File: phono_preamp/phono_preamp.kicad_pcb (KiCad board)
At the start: 2 copper layers, 30 parts, among them U1 NE5532, U2 NE5532

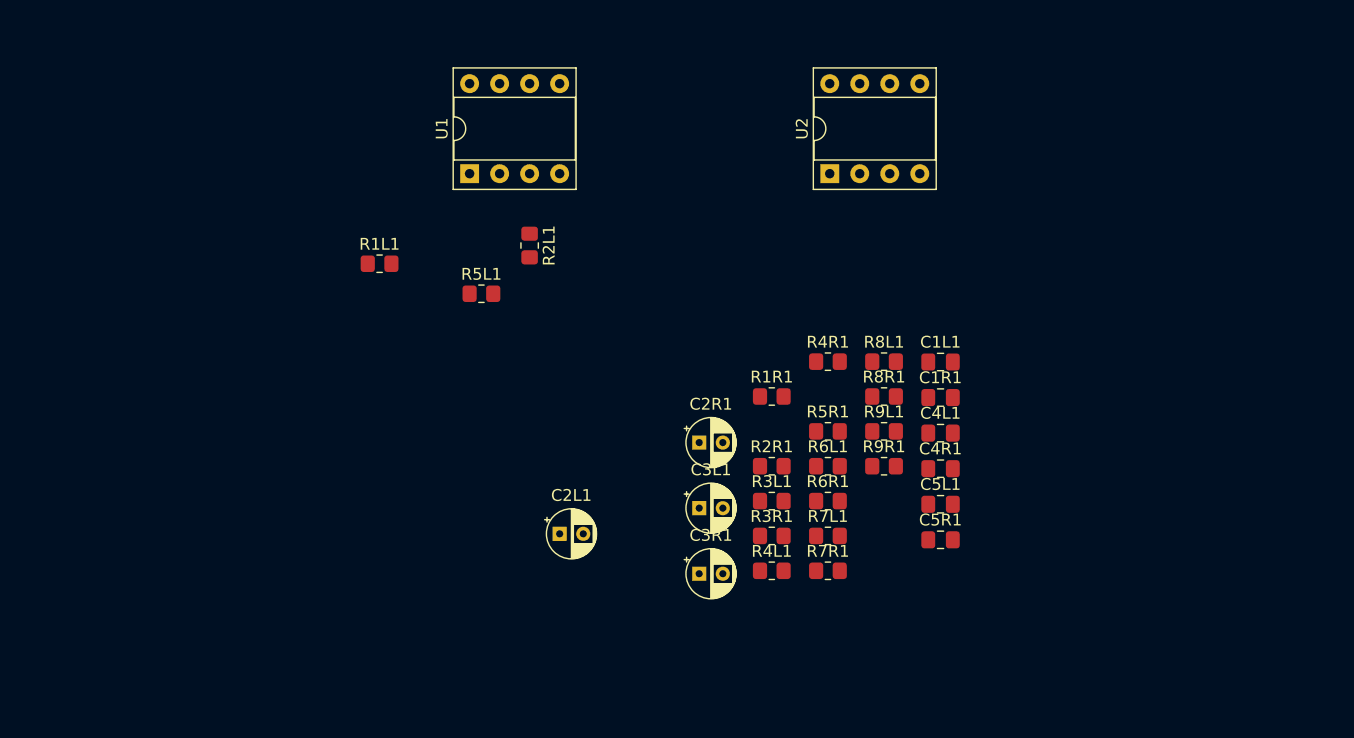
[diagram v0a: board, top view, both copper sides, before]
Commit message: testing some routing options
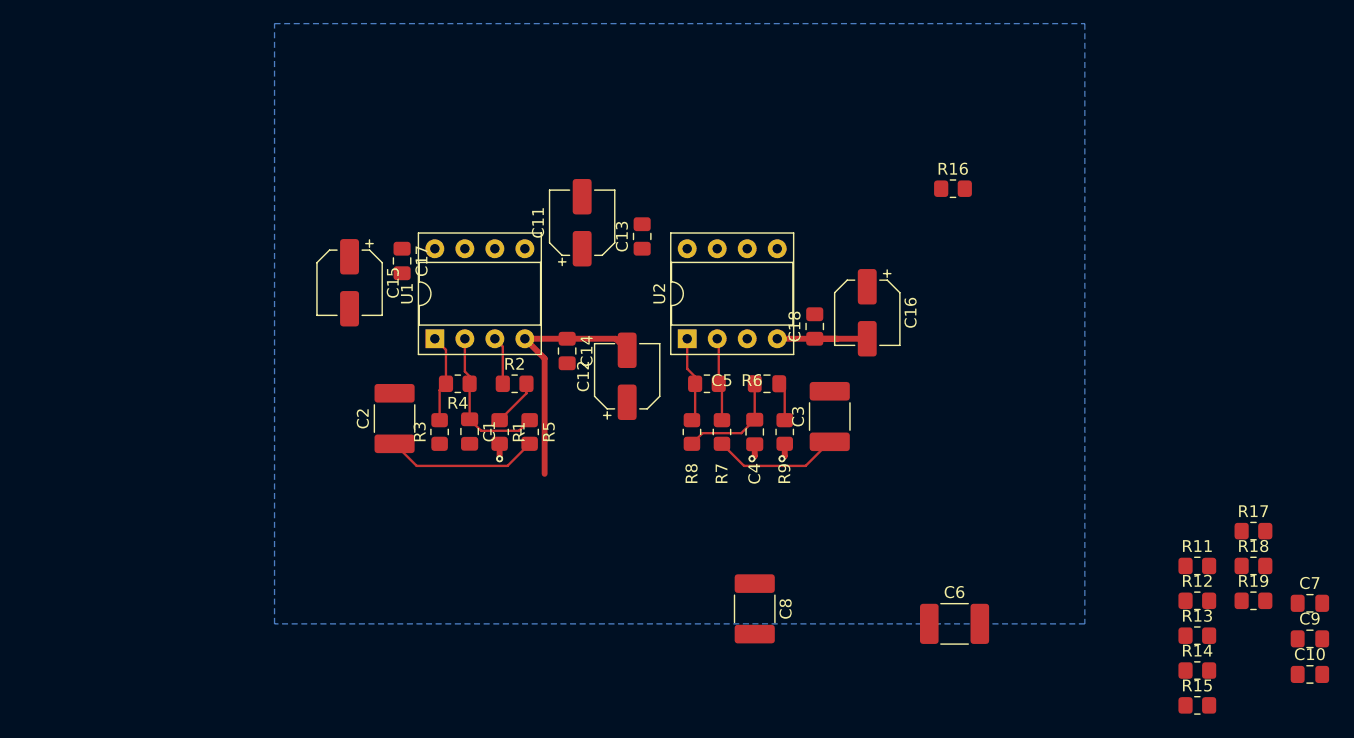
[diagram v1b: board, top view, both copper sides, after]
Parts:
- removed C1L1, C1R1: 22n, Capacitor_SMD:C_0805_2012Metric_Pad1.18x1.45mm_HandSolder
- removed C2L1, C2R1, C3L1, C3R1: 22u, Capacitor_THT:CP_Radial_D4.0mm_P2.00mm
- removed C4L1, C4R1: 100n, Capacitor_SMD:C_0805_2012Metric_Pad1.18x1.45mm_HandSolder
- removed C5L1, C5R1: 1u, Capacitor_SMD:C_0805_2012Metric_Pad1.18x1.45mm_HandSolder
- removed R1L1, R1R1: 47k, Resistor_SMD:R_0805_2012Metric_Pad1.20x1.40mm_HandSolder
- removed R2L1, R2R1: 2k2, Resistor_SMD:R_0805_2012Metric_Pad1.20x1.40mm_HandSolder
- removed R3L1, R3R1: 10k, Resistor_SMD:R_0805_2012Metric_Pad1.20x1.40mm_HandSolder
- removed R4L1, R4R1: 180k, Resistor_SMD:R_0805_2012Metric_Pad1.20x1.40mm_HandSolder
- removed R5L1, R5R1: 4k7, Resistor_SMD:R_0805_2012Metric_Pad1.20x1.40mm_HandSolder
- removed R6L1, R6R1, R9L1, R9R1: 100k, Resistor_SMD:R_0805_2012Metric_Pad1.20x1.40mm_HandSolder
- removed R7L1, R7R1: 2k7, Resistor_SMD:R_0805_2012Metric_Pad1.20x1.40mm_HandSolder
- removed R8L1, R8R1: 750, Resistor_SMD:R_0805_2012Metric_Pad1.20x1.40mm_HandSolder
- added C1: 22n, Capacitor_SMD:C_0805_2012Metric_Pad1.18x1.45mm_HandSolder, F.Cu at (55.9, 62.5)
- added C10: 1u, Capacitor_SMD:C_0805_2012Metric_Pad1.18x1.45mm_HandSolder, F.Cu at (127.0, 83.0)
- added C11: 10u, Capacitor_SMD:CP_Elec_5x5.9, F.Cu at (65.4, 44.8)
- added C12: 10u, Capacitor_SMD:CP_Elec_5x5.9, F.Cu at (69.2, 57.8)
- added C13: 100n, Capacitor_SMD:C_0805_2012Metric_Pad1.18x1.45mm_HandSolder, F.Cu at (70.5, 46.0)
- added C14: 100n, Capacitor_SMD:C_0805_2012Metric_Pad1.18x1.45mm_HandSolder, F.Cu at (64.1, 55.6)
- added C15: 10u, Capacitor_SMD:CP_Elec_5x5.9, F.Cu at (45.7, 49.9)
- added C16: 10u, Capacitor_SMD:CP_Elec_5x5.9, F.Cu at (89.5, 52.4)
- added C17: 100n, Capacitor_SMD:C_0805_2012Metric_Pad1.18x1.45mm_HandSolder, F.Cu at (50.2, 48.0)
- added C18: 100n, Capacitor_SMD:C_0805_2012Metric_Pad1.18x1.45mm_HandSolder, F.Cu at (85.1, 53.6)
- added C2: 22u, Capacitor_SMD:C_1812_4532Metric_Pad1.57x3.40mm_HandSolder, F.Cu at (49.5, 61.4)
- added C3: 22u, Capacitor_SMD:C_1812_4532Metric_Pad1.57x3.40mm_HandSolder, F.Cu at (86.4, 61.2)
- added C4: 100n, Capacitor_SMD:C_0805_2012Metric_Pad1.18x1.45mm_HandSolder, F.Cu at (80.0, 62.5)
- added C5: 1u, Capacitor_SMD:C_0805_2012Metric_Pad1.18x1.45mm_HandSolder, F.Cu at (81.0, 58.4)
- added C6: 22u, Capacitor_SMD:C_1812_4532Metric_Pad1.57x3.40mm_HandSolder, F.Cu at (96.9, 78.7)
- added C7: 22n, Capacitor_SMD:C_0805_2012Metric_Pad1.18x1.45mm_HandSolder, F.Cu at (127.0, 77.0)
- added C8: 22u, Capacitor_SMD:C_1812_4532Metric_Pad1.57x3.40mm_HandSolder, F.Cu at (80.0, 77.5)
- added C9: 100n, Capacitor_SMD:C_0805_2012Metric_Pad1.18x1.45mm_HandSolder, F.Cu at (127.0, 80.0)
- added R1: 47k, Resistor_SMD:R_0805_2012Metric_Pad1.20x1.40mm_HandSolder, F.Cu at (58.4, 62.5)
- added R11: 47k, Resistor_SMD:R_0805_2012Metric_Pad1.20x1.40mm_HandSolder, F.Cu at (117.5, 73.8)
- added R12: 2k2, Resistor_SMD:R_0805_2012Metric_Pad1.20x1.40mm_HandSolder, F.Cu at (117.5, 76.8)
- added R13: 4k7, Resistor_SMD:R_0805_2012Metric_Pad1.20x1.40mm_HandSolder, F.Cu at (117.5, 79.7)
- added R14: 180k, Resistor_SMD:R_0805_2012Metric_Pad1.20x1.40mm_HandSolder, F.Cu at (117.5, 82.7)
- added R15: 10k, Resistor_SMD:R_0805_2012Metric_Pad1.20x1.40mm_HandSolder, F.Cu at (117.5, 85.6)
- added R16: 2k7, Resistor_SMD:R_0805_2012Metric_Pad1.20x1.40mm_HandSolder, F.Cu at (96.8, 41.9)
- added R17: 100k, Resistor_SMD:R_0805_2012Metric_Pad1.20x1.40mm_HandSolder, F.Cu at (122.2, 70.9)
- added R18: 750, Resistor_SMD:R_0805_2012Metric_Pad1.20x1.40mm_HandSolder, F.Cu at (122.2, 73.8)
- added R19: 100k, Resistor_SMD:R_0805_2012Metric_Pad1.20x1.40mm_HandSolder, F.Cu at (122.2, 76.8)
- added R2: 2k2, Resistor_SMD:R_0805_2012Metric_Pad1.20x1.40mm_HandSolder, F.Cu at (59.7, 58.4)
- added R3: 10k, Resistor_SMD:R_0805_2012Metric_Pad1.20x1.40mm_HandSolder, F.Cu at (53.3, 62.5)
- added R4: 180k, Resistor_SMD:R_0805_2012Metric_Pad1.20x1.40mm_HandSolder, F.Cu at (54.9, 58.4)
- added R5: 4k7, Resistor_SMD:R_0805_2012Metric_Pad1.20x1.40mm_HandSolder, F.Cu at (61.0, 62.5)
- added R6: 100k, Resistor_SMD:R_0805_2012Metric_Pad1.20x1.40mm_HandSolder, F.Cu at (76.0, 58.4)
- added R7: 2k7, Resistor_SMD:R_0805_2012Metric_Pad1.20x1.40mm_HandSolder, F.Cu at (77.2, 62.5)
- added R8: 750, Resistor_SMD:R_0805_2012Metric_Pad1.20x1.40mm_HandSolder, F.Cu at (74.7, 62.5)
- added R9: 100k, Resistor_SMD:R_0805_2012Metric_Pad1.20x1.40mm_HandSolder, F.Cu at (82.5, 62.5)
- moved U2 18.5 mm to (74.3, 54.6)
- moved U1 14.3 mm to (52.9, 54.6)
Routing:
- net -15V: track 0.00 -> 30.7 mm
- net Net-(C2-Pad1): track 0.00 -> 13.0 mm
- net Net-(U1A--): track 0.00 -> 12.8 mm
- net Net-(C3-Pad1): track 0.00 -> 10.7 mm
- net Net-(C4-Pad1): track 0.00 -> 9.20 mm
- net Net-(U2A-+): track 0.00 -> 7.50 mm
- net Net-(R6-Pad2): track 0.00 -> 7.28 mm
- net Net-(U2A--): track 0.00 -> 7.06 mm
- net Net-(U1A-+): track 0.00 -> 4.09 mm
- net /IN_L: track 0.00 -> 4.02 mm
- net GND: track 0.00 -> 3.97 mm, vias 0 -> 3
- net /OUT_L: track 0.00 -> 3.27 mm
- added copper zone on B.Cu, net GND

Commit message: cleanup placement
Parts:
- moved R4 26.3 mm to (29.2, 52.7)
- moved C2 26.1 mm to (24.1, 55.2)
- moved C4 26.1 mm to (54.6, 56.5)
- moved R8 26.1 mm to (49.3, 56.5)
- moved C1 26.1 mm to (30.5, 56.5)
- moved R3 26.1 mm to (27.9, 56.5)
- moved R1 26.1 mm to (33.0, 56.5)
- moved R5 26.1 mm to (35.6, 56.5)
- moved R7 26.1 mm to (51.8, 56.5)
- moved R9 26.1 mm to (57.1, 56.5)
- moved C3 26.1 mm to (61.0, 55.2)
- moved C5 26.0 mm to (55.6, 52.7)
- moved R2 26.0 mm to (34.3, 52.7)
- moved R6 26.0 mm to (50.6, 52.7)
- moved C12 25.4 mm to (44.5, 52.1)
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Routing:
- net -15V: track 30.7 -> 0.00 mm
- net Net-(C2-Pad1): track 13.0 -> 0.00 mm
- net Net-(U1A--): track 12.8 -> 0.42 mm
- net Net-(C3-Pad1): track 10.7 -> 0.00 mm
- net Net-(C4-Pad1): track 9.20 -> 0.00 mm
- net Net-(U2A-+): track 7.50 -> 0.00 mm
- net Net-(R6-Pad2): track 7.28 -> 0.00 mm
- net Net-(U2A--): track 7.06 -> 0.00 mm
- net Net-(U1A-+): track 4.09 -> 0.00 mm
- net /IN_L: track 4.02 -> 0.00 mm
- net /OUT_L: track 3.27 -> 0.00 mm
- net GND: track 3.97 -> 1.87 mm

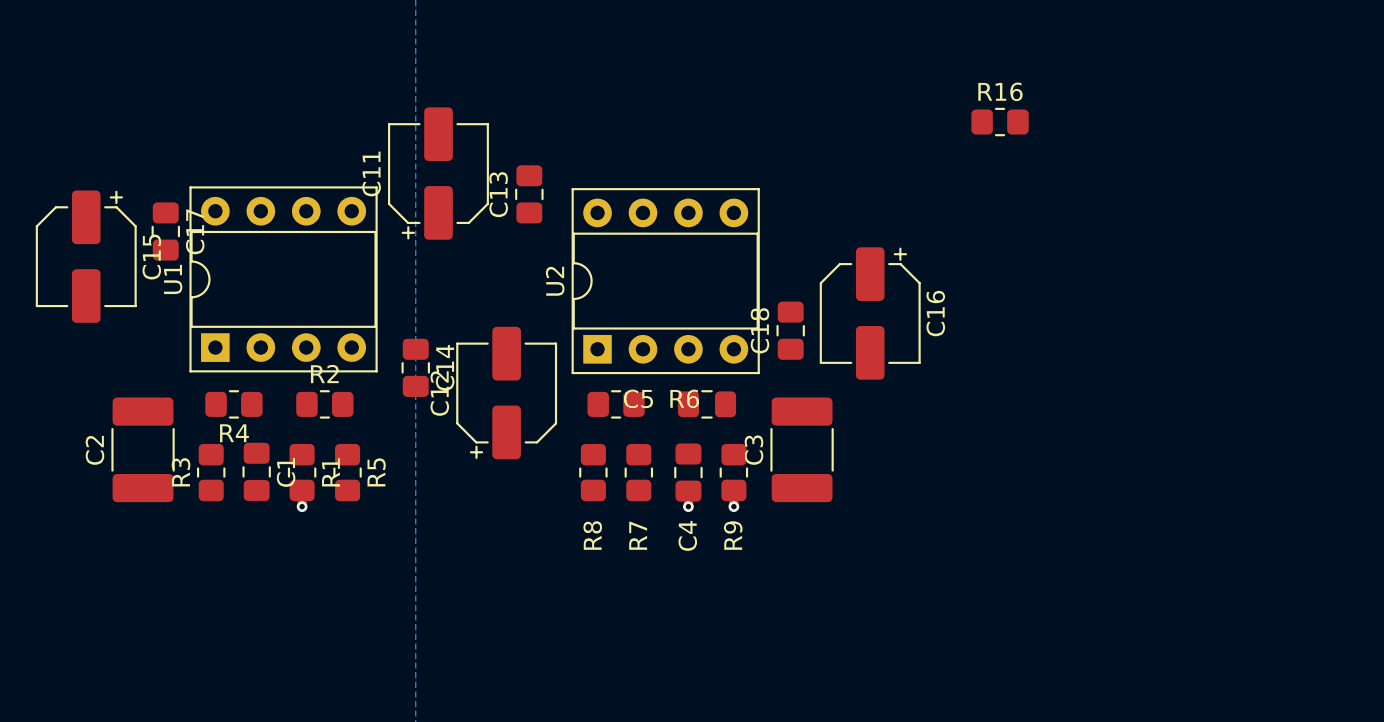
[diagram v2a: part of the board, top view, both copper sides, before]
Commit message: change big bypass caps to ceramic
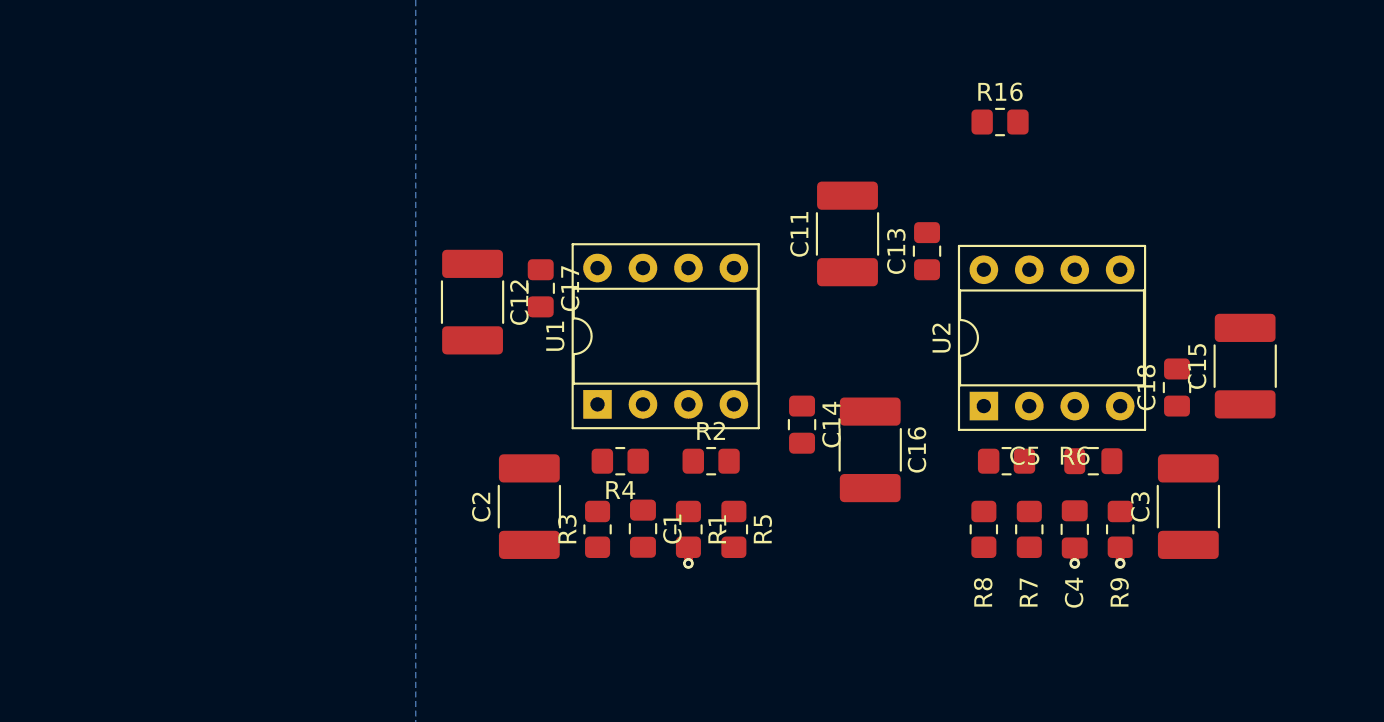
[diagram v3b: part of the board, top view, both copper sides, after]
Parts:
- C11, C12, C15, C16: value 10u -> 22u; footprint Capacitor_SMD:CP_Elec_5x5.9 -> Capacitor_SMD:C_1812_4532Metric_Pad1.57x3.40mm_HandSolder
- moved C15 65.1 mm to (85.7, 50.6), turned to 90 degrees
- moved C11 23.1 mm to (63.5, 43.2)
- moved C13 22.5 mm to (67.9, 44.1)
- moved R6 22.1 mm to (72.4, 55.9)
- moved R8 22.1 mm to (71.1, 59.7)
- moved R7 22.1 mm to (73.7, 59.7)
- moved C14 21.8 mm to (61.0, 53.8)
- moved C18 21.8 mm to (81.9, 51.8)
- moved C4 21.8 mm to (76.2, 59.7)
- moved R2 21.8 mm to (55.9, 55.9)
- moved U2 21.8 mm to (71.1, 52.8)
- moved C1 21.8 mm to (52.1, 59.7)
- moved C2 21.8 mm to (45.7, 58.4)
- moved R3 21.8 mm to (49.5, 59.7)
- moved C3 21.8 mm to (82.5, 58.4)
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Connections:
- C12 pad 1: GND -> +15V
- C12 pad 2: -15V -> GND
- C15 pad 1: +15V -> -15V
- C16 pad 1: GND -> -15V
- C16 pad 2: -15V -> GND
